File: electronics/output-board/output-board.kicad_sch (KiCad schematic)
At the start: 0 parts

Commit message: Added BSS806N library to the output board
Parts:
- added MOSFET?: BSS806NEH6327XTSA1, PG-SOT23-3-5_INF, symbol 2021-09-18_15-04-13:BSS806NEH6327XTSA1
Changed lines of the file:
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@@
 (kicad_sch (version 20210621) (generator eeschema)
   (paper "A4")
-  (symbol_instances)
+  (symbol (lib_id "2021-09-18_15-04-13:BSS806NEH6327XTSA1") (at 63.5 39.37 90) (unit 1)
+    (in_bom yes) (on_board yes) (fields_autoplaced)
+    (property "Reference" "MOSFET?" (id 0) (at 63.5 19.599 90)
+      (effects (font (size 1.524 1.524)))
+    )
+    (property "Value" "BSS806NEH6327XTSA1" (id 1) (at 63.5 22.878 90)
+      (effects (font (size 1.524 1.524)))
+    )
+    (property "Footprint" "PG-SOT23-3-5_INF" (id 2) (at 70.104 27.94 0)
+      (effects (font (size 1.524 1.524)) hide)
+    )
+    (property "Datasheet" "" (id 3) (at 63.5 39.37 0)
+      (effects (font (size 1.524 1.524)))
+    )
+    (pin "1")
+    (pin "2")
+    (pin "3")
+  )
+  (sheet_instances
+    (path "/" (page "1"))
+  )
+  (symbol_instances
+    (path "/b31e6aa4-4d79-4fd3-a6f6-5de1c4b80e42"
+      (reference "MOSFET?") (unit 1) (value "BSS806NEH6327XTSA1") (footprint "PG-SOT23-3-5_INF")
+    )
+  )
 )

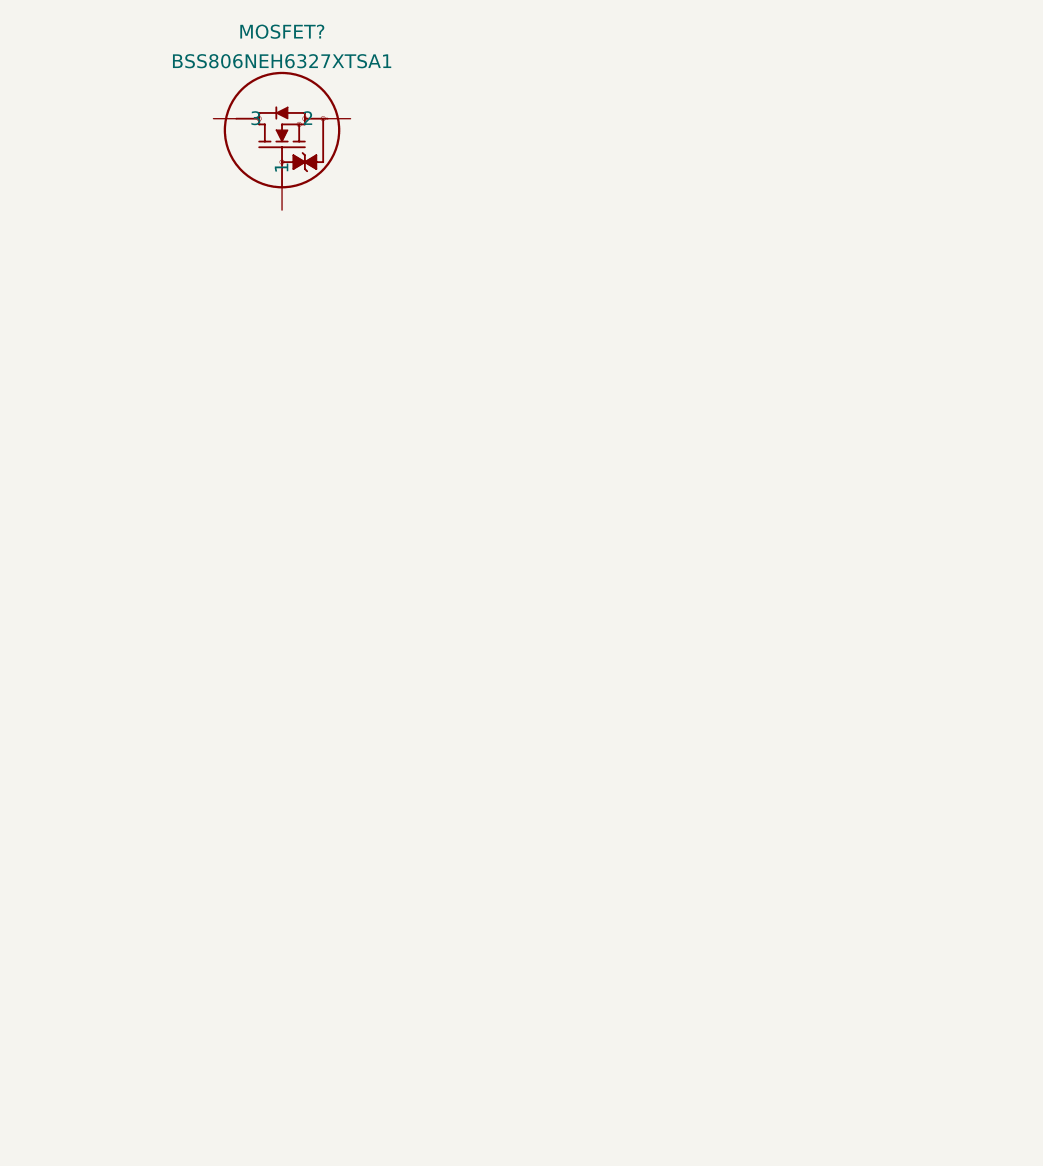
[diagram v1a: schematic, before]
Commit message: started working on output board
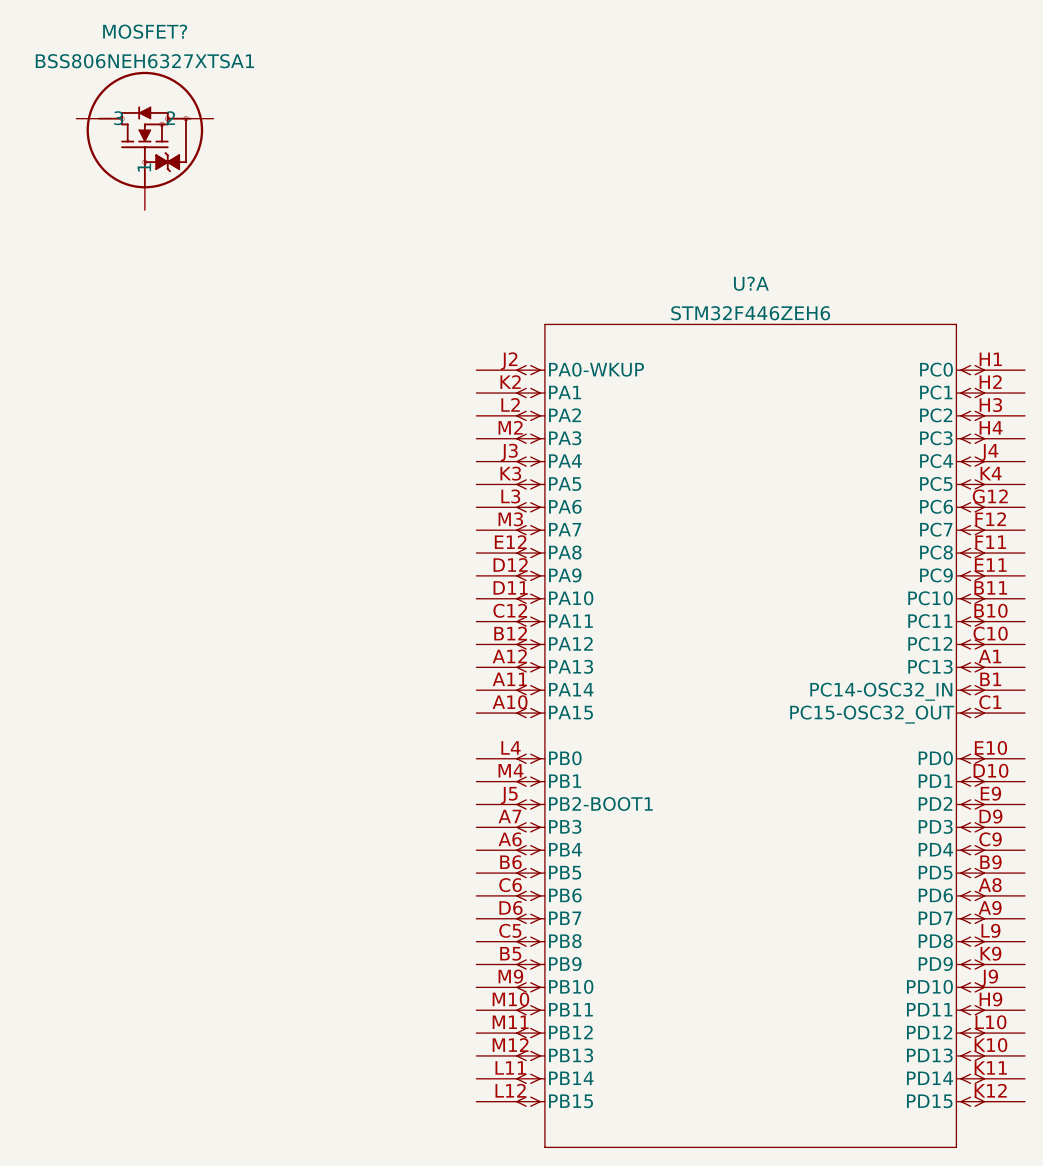
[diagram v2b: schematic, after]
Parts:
- added U?: STM32F446ZEH6, UFBGA144-7x7x0P6, symbol 2021-09-18_15-12-50:STM32F446ZEH6
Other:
- moved on the sheet: MOSFET?
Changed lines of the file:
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@@
 (kicad_sch (version 20210621) (generator eeschema)
   (paper "A4")
-  (symbol (lib_id "2021-09-18_15-04-13:BSS806NEH6327XTSA1") (at 63.5 39.37 90) (unit 1)
+  (symbol (lib_id "2021-09-18_15-04-13:BSS806NEH6327XTSA1") (at 48.26 39.37 90) (unit 1)
     (in_bom yes) (on_board yes) (fields_autoplaced)
-    (property "Reference" "MOSFET?" (id 0) (at 63.5 19.599 90)
+    (property "Reference" "MOSFET?" (id 0) (at 48.26 19.599 90)
       (effects (font (size 1.524 1.524)))
     )
-    (property "Value" "BSS806NEH6327XTSA1" (id 1) (at 63.5 22.878 90)
+    (property "Value" "BSS806NEH6327XTSA1" (id 1) (at 48.26 22.878 90)
       (effects (font (size 1.524 1.524)))
     )
-    (property "Footprint" "PG-SOT23-3-5_INF" (id 2) (at 70.104 27.94 0)
+    (property "Footprint" "PG-SOT23-3-5_INF" (id 2) (at 54.864 27.94 0)
       (effects (font (size 1.524 1.524)) hide)
     )
-    (property "Datasheet" "" (id 3) (at 63.5 39.37 0)
+    (property "Datasheet" "" (id 3) (at 48.26 39.37 0)
       (effects (font (size 1.524 1.524)))
     )
@@
     (pin "2")
     (pin "3")
+  )
+  (symbol (lib_id "2021-09-18_15-12-50:STM32F446ZEH6") (at 85.09 57.15 0) (unit 1)
+    (in_bom yes) (on_board yes) (fields_autoplaced)
+    (property "Reference" "U?" (id 0) (at 115.57 47.6025 0)
+      (effects (font (size 1.524 1.524)))
+    )
+    (property "Value" "STM32F446ZEH6" (id 1) (at 115.57 50.8815 0)
+      (effects (font (size 1.524 1.524)))
+    )
+    (property "Footprint" "UFBGA144-7x7x0P6" (id 2) (at 115.57 51.054 0)
+      (effects (font (size 1.524 1.524)) hide)
+    )
+    (property "Datasheet" "" (id 3) (at 85.09 57.15 0)
+      (effects (font (size 1.524 1.524)))
+    )
+    (pin "A1")
+    (pin "A10")
+    (pin "A11")
+    (pin "A12")
+    (pin "A6")
+    (pin "A7")
+    (pin "A8")
+    (pin "A9")
+    (pin "B1")
+    (pin "B10")
+    (pin "B11")
+    (pin "B12")
+    (pin "B5")
+    (pin "B6")
+    (pin "B9")
+    (pin "C1")
+    (pin "C10")
+    (pin "C12")
+    (pin "C5")
+    (pin "C6")
+    (pin "C9")
+    (pin "D10")
+    (pin "D11")
+    (pin "D12")
+    (pin "D6")
+    (pin "D9")
+    (pin "E10")
+    (pin "E11")
+    (pin "E12")
+    (pin "E9")
+    (pin "F11")
+    (pin "F12")
+    (pin "G12")
+    (pin "H1")
+    (pin "H2")
+    (pin "H3")
+    (pin "H4")
+    (pin "H9")
+    (pin "J2")
+    (pin "J3")
+    (pin "J4")
+    (pin "J5")
+    (pin "J9")
+    (pin "K10")
+    (pin "K11")
+    (pin "K12")
+    (pin "K2")
+    (pin "K3")
+    (pin "K4")
+    (pin "K9")
+    (pin "L10")
+    (pin "L11")
+    (pin "L12")
+    (pin "L2")
+    (pin "L3")
+    (pin "L4")
+    (pin "L9")
+    (pin "M10")
+    (pin "M11")
+    (pin "M12")
+    (pin "M2")
+    (pin "M3")
+    (pin "M4")
+    (pin "M9")
   )
   (sheet_instances
@@
       (reference "MOSFET?") (unit 1) (value "BSS806NEH6327XTSA1") (footprint "PG-SOT23-3-5_INF")
     )
+    (path "/e354fa5f-e405-4e62-b4d4-c6e5e046a118"
+      (reference "U?") (unit 1) (value "STM32F446ZEH6") (footprint "UFBGA144-7x7x0P6")
+    )
   )

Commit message: Added MOSFETS to the output board.
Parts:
- removed U?: STM32F446ZEH6, UFBGA144-7x7x0P6, symbol 2021-09-18_15-12-50:STM32F446ZEH6
- added D?: LED, symbol Device:LED
- added J1, J? (x16): Conn_01x02_Male, symbol Connector:Conn_01x02_Male
- added MOSFET? (x16): BSS806NEH6327XTSA1, PG-SOT23-3-5_INF, symbol 2021-09-18_15-04-13:BSS806NEH6327XTSA1
- added Q?: 2N2219, Package_TO_SOT_THT:TO-39-3, symbol Transistor_BJT:2N2219
- added R? (x18): R, symbol Device:R
- gave numbers to parts that had none: 1
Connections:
- net at MOSFET1.1: now also Q?.2 (B), R?.1
- net GND: now reaches MOSFET1.2
- net GND: now also MOSFET?.2, MOSFET?.2, MOSFET?.2, MOSFET?.2, MOSFET?.2, MOSFET?.2, MOSFET?.2, MOSFET?.2, MOSFET?.2, MOSFET?.2, MOSFET?.2, MOSFET?.2, MOSFET?.2, R?.2
- net at MOSFET1.3: now also J1.1 (Pin_1)
- new net: MOSFET?.1, R?.1 (x16)
- new net: J?.1 (Pin_1), MOSFET?.3 (x15)
- new net: Q?.1 (E), R?.1
- new net: MOSFET?.2, MOSFET?.2, MOSFET?.2, MOSFET?.3
- new net: J?.1 (Pin_1), R?.2
- new net: D?.1 (K), Q?.3 (C)
- new net +12V: J1.2 (Pin_2), J?.2 (Pin_2), J?.2 (Pin_2), J?.2 (Pin_2), J?.2 (Pin_2), J?.2 (Pin_2), J?.2 (Pin_2), J?.2 (Pin_2), J?.2 (Pin_2), J?.2 (Pin_2), J?.2 (Pin_2), J?.2 (Pin_2), J?.2 (Pin_2), J?.2 (Pin_2), J?.2 (Pin_2), J?.2 (Pin_2)
- new net +5V: D?.2 (A)
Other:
- note added: "Arming Switch"
- note added: "Do I need a pulldown resistor?"
- moved on the sheet: MOSFET1

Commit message: Finished Schematic and Started Routing the Output Board
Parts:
- removed D?: LED, symbol Device:LED
- removed J1, J? (x16): Conn_01x02_Male, symbol Connector:Conn_01x02_Male
- removed MOSFET1, MOSFET? (x16): BSS806NEH6327XTSA1, PG-SOT23-3-5_INF, symbol 2021-09-18_15-04-13:BSS806NEH6327XTSA1
- removed Q?: 2N2219, Package_TO_SOT_THT:TO-39-3, symbol Transistor_BJT:2N2219
- removed R? (x18): R, symbol Device:R
- added C1, C3: 1uF, Capacitor_SMD:C_0603_1608Metric, symbol Device:C_Small
- added C10, C11, C12, C13, C14, C15, C16, C17, C18, C19, C20, C21, C6, C9: 100nF, Capacitor_SMD:C_0603_1608Metric, symbol Device:C_Small
- added C2: 10nF, Capacitor_SMD:C_0603_1608Metric, symbol Device:C_Small
- added C4, C5: 20pF, Capacitor_SMD:C_0603_1608Metric, symbol Device:C_Small
- added C7, C8: 2.2uF, Capacitor_SMD:C_0603_1608Metric, symbol Device:C_Small
- added J14: Arming switch, Connector_PinHeader_2.54mm:PinHeader_1x02_P2.54mm_Vertical, symbol Connector:Conn_01x02_Male
- added J3: 12V In, Connector_PinHeader_2.54mm:PinHeader_1x02_P2.54mm_Vertical, symbol Connector:Conn_01x02_Male
- added J4, J6: Conn_01x02, Connector_PinHeader_2.54mm:PinHeader_1x02_P2.54mm_Vertical, symbol Connector_Generic:Conn_01x02
- added J5: SWD Header, Connector_PinHeader_2.54mm:PinHeader_1x04_P2.54mm_Vertical, symbol Connector_Generic:Conn_01x04
- added L1: 10uH, Inductor_SMD:L_0603_1608Metric, symbol Device:L_Core_Iron
- added MOSFET10: BUK9Y21-40E, MOSFET 2:BUK9Y21-40E, symbol ArmingMOSFET:BUK9Y21-40E
- added R1: 0k, Resistor_SMD:R_0603_1608Metric, symbol Device:R_Small
- added R12: 1K, Resistor_SMD:R_0603_1608Metric, symbol Device:R
- added R13: 100K, Resistor_SMD:R_0603_1608Metric, symbol Device:R
- added R3: 10k, Resistor_SMD:R_0603_1608Metric, symbol Device:R_Small
- added SW1: SW_Push_Dual, RESET BUTTON:Button CS1102, symbol Switch:SW_Push_Dual
- added U1: MAX33012EASA+, MAX33012EASA+:MAX33012EASA+, symbol MAX33012EASA+:MAX33012EASA+
- added U2: LD3985M33R_SOT23, Package_TO_SOT_SMD:SOT-23-5, symbol Regulator_Linear:LD3985M33R_SOT23
- added U3: STM32F446ZEHx, Package_BGA:UFBGA-144_7x7mm_Layout12x12_P0.5mm, symbol MCU_ST_STM32F4:STM32F446ZEHx
- added Y1: 25MHz 9pF, symbol Device:Crystal_Small
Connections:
- net +12V: now also J3.2 (Pin_2)
- net +5V: now also C1.1, J14.2 (Pin_2), J4.1 (Pin_1), J5.2 (Pin_2), U2.1 (VIN), U2.3 (INH)
- net GND: now also C1.2, C10.2, C11.2, C12.2, C13.2, C14.2, C15.2, C16.2, C17.2, C18.2, C19.2, C2.2, C20.2, C21.2, C3.2, C4.1, C5.1, C6.1, C7.2, C8.2, C9.2, J3.1 (Pin_1), J4.2 (Pin_2), J5.1 (Pin_1), MOSFET10.1, MOSFET10.2, MOSFET10.3, R13.2, R3.2, SW1.1, SW1.3, U1.2 (GND), U1.8 (STBY), U2.2 (GND), U3.D2 (VSS), U3.E6 (VSS), U3.E7 (VSS), U3.G10 (VSS), U3.G4 (VSS), U3.G8 (VSS), U3.H6 (VSS), U3.J1 (VSSA), U3.K1 (VREF-)
- new net: MOSFET10.4, R12.1
- new net: C6.2, SW1.2, SW1.4, U3.F1 (NRST)
- new net: J14.1 (Pin_1), R12.2, R13.1, U3.C3 (PF0)
- new net: J6.2 (Pin_2), U1.6 (CANL)
- new net: J6.1 (Pin_1), U1.7 (CANH)
- new net: C5.2, U3.E1 (PH1), Y1.1
- new net: C2.1, U2.4 (BYP)
- new net: C4.2, R1.1, Y1.2
- new net: R3.1, U3.D5 (BOOT0)
- new net: C8.1, U3.G9 (VCAP_2)
- new net: C7.1, U3.H7 (VCAP_1)
- new net: R1.2, U3.D1 (PH0)
- new net +3V3: C11.1, C12.1, C13.1, C14.1, C15.1, C16.1, C17.1, C18.1, C19.1, C20.1, C21.1, C3.1, C9.1, L1.2, U1.3 (VDD), U2.5 (VOUT), U3.C2 (VBAT), U3.D3 (VDD), U3.E5 (PDR_ON), U3.F10 (VDD), U3.F4 (VDD), U3.F5 (VDD), U3.F6 (VDD), U3.F7 (VDD), U3.F8 (VDD), U3.F9 (VDD), U3.G5 (VDD), U3.G6 (VDD), U3.G7 (VDD)
- new net CAN_RX: U1.4 (RXD), U3.E10 (PD0)
- new net CAN_TX: U1.1 (TXD), U3.D10 (PD1)
- new net Ignition MOSFET/GROUND: MOSFET10.5
- new net Ignition MOSFET/INPUT: U3.B8 (PG12)
- new net MOSFET-sheet/INPUT: U3.K6 (PG0)
- new net MOSFET-sheet1/INPUT: U3.J6 (PG1)
- new net MOSFET-sheet10/INPUT: U3.D8 (PG10)
- new net MOSFET-sheet11/INPUT: U3.C8 (PG11)
- new net MOSFET-sheet2/INPUT: U3.J12 (PG2)
- new net MOSFET-sheet3/INPUT: U3.J11 (PG3)
- new net MOSFET-sheet4/INPUT: U3.J10 (PG4)
- new net MOSFET-sheet5/INPUT: U3.H12 (PG5)
- new net MOSFET-sheet6/INPUT: U3.H11 (PG6)
- new net MOSFET-sheet7/INPUT: U3.H10 (PG7)
- new net MOSFET-sheet8/INPUT: U3.G11 (PG8)
- new net MOSFET-sheet9/INPUT: U3.E8 (PG9)
- new net SWCLK: J5.3 (Pin_3), U3.A11 (PA14)
- new net SWDIO: J5.4 (Pin_4), U3.A12 (PA13)
- new net VDDA: C10.1, L1.1, U3.L1 (VREF+), U3.M1 (VDDA)
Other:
- added sheet Ignition MOSFET (untitled.kicad_sch)
- added sheet MOSFET-sheet (untitled.kicad_sch)
- added sheet MOSFET-sheet1 (untitled.kicad_sch)
- added sheet MOSFET-sheet10 (untitled.kicad_sch)
- added sheet MOSFET-sheet11 (untitled.kicad_sch)
- added sheet MOSFET-sheet2 (untitled.kicad_sch)
- added sheet MOSFET-sheet3 (untitled.kicad_sch)
- added sheet MOSFET-sheet4 (untitled.kicad_sch)
- added sheet MOSFET-sheet5 (untitled.kicad_sch)
- added sheet MOSFET-sheet6 (untitled.kicad_sch)
- added sheet MOSFET-sheet7 (untitled.kicad_sch)
- added sheet MOSFET-sheet8 (untitled.kicad_sch)
- added sheet MOSFET-sheet9 (untitled.kicad_sch)
- note added: "Each VDD pin should be connected to a decoupling capacitor as closely as possible to the pin"
- note added: "Hardcode to boot from flash memory"
- note added: "Should be ceramic capacitors (low ESR)"
- note added: "To Do: -Servo Valve Control? -Layout Board -Get Footprints"
- note removed: "Arming Switch"
- note removed: "Do I need a pulldown resistor?"

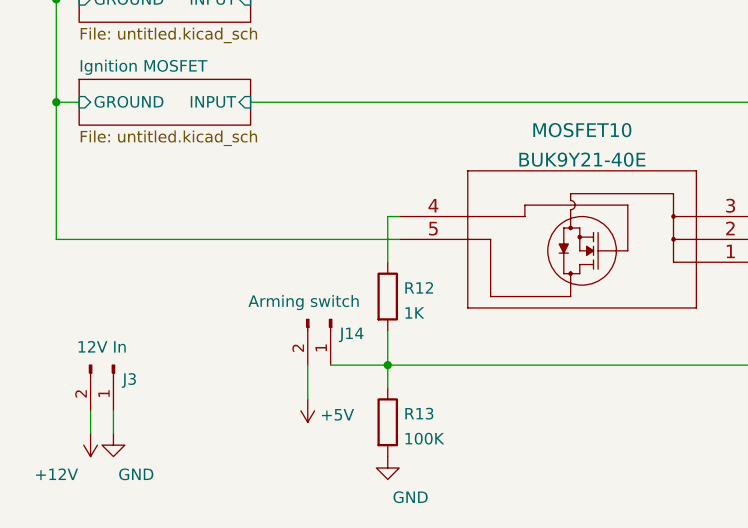
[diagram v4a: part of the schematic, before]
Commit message: Working on ouput board.
Saving before using the replicate layout plugin.
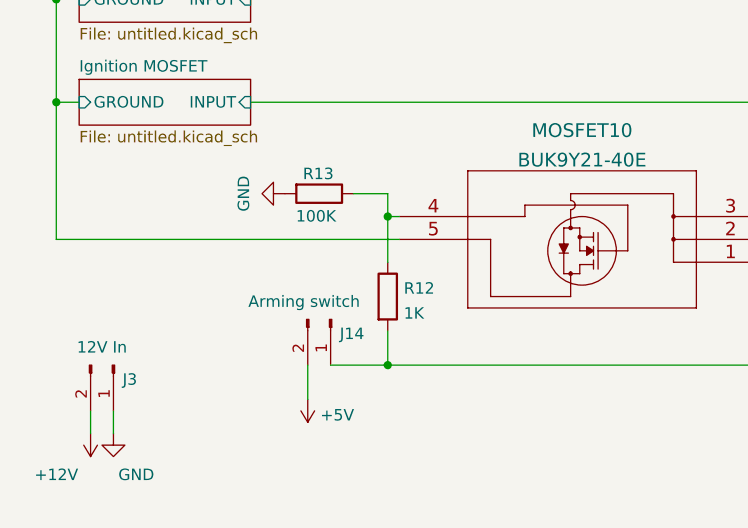
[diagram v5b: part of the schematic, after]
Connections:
- net at MOSFET10.4, R12.1: now also R13.1
- net at J14.1 (Pin_1), R12.2, U3.C3 (PF0): no longer R13.1
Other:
- moved on the sheet: R13
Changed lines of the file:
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@@
   (junction (at 53.34 55.88) (diameter 1.016) (color 0 0 0 0))
   (junction (at 62.23 55.88) (diameter 1.016) (color 0 0 0 0))
+  (junction (at 63.5 302.26) (diameter 0) (color 0 0 0 0))
   (junction (at 63.5 318.77) (diameter 0) (color 0 0 0 0))
   (junction (at 69.85 45.72) (diameter 0) (color 0 0 0 0))
@@
     (stroke (width 0) (type default) (color 0 0 0 0))
   )
+  (wire (pts (xy 59.69 299.72) (xy 63.5 299.72))
+    (stroke (width 0) (type default) (color 0 0 0 0))
+  )
   (wire (pts (xy 60.96 45.72) (xy 69.85 45.72))
     (stroke (width 0) (type solid) (color 0 0 0 0))
@@
     (stroke (width 0) (type solid) (color 0 0 0 0))
   )
+  (wire (pts (xy 63.5 299.72) (xy 63.5 302.26))
+    (stroke (width 0) (type default) (color 0 0 0 0))
+  )
   (wire (pts (xy 63.5 302.26) (xy 63.5 307.34))
     (stroke (width 0) (type default) (color 0 0 0 0))
@@
   )
   (wire (pts (xy 63.5 314.96) (xy 63.5 318.77))
-    (stroke (width 0) (type default) (color 0 0 0 0))
-  )
-  (wire (pts (xy 63.5 318.77) (xy 63.5 321.31))
     (stroke (width 0) (type default) (color 0 0 0 0))
   )
@@
     (pin "1")
   )
+  (symbol (lib_id "power:GND") (at 52.07 299.72 270) (unit 1)
+    (in_bom yes) (on_board yes)
+    (property "Reference" "#PWR0103" (id 0) (at 45.72 299.72 0)
+      (effects (font (size 1.27 1.27)) hide)
+    )
+    (property "Value" "GND" (id 1) (at 47.5074 299.72 0))
+    (property "Footprint" "" (id 2) (at 52.07 299.72 0)
+      (effects (font (size 1.27 1.27)) hide)
+    )
+    (property "Datasheet" "" (id 3) (at 52.07 299.72 0)
+      (effects (font (size 1.27 1.27)) hide)
+    )
+    (pin "1")
+  )
   (symbol (lib_id "power:GND") (at 53.34 55.88 0) (unit 1)
     (in_bom yes) (on_board yes) (fields_autoplaced)
@@
     )
     (property "Datasheet" "" (id 3) (at 57.15 109.22 0)
-      (effects (font (size 1.27 1.27)) hide)
-    )
-    (pin "1")
-  )
-  (symbol (lib_id "power:GND") (at 63.5 328.93 0) (unit 1)
-    (in_bom yes) (on_board yes)
-    (property "Reference" "#PWR0103" (id 0) (at 63.5 335.28 0)
-      (effects (font (size 1.27 1.27)) hide)
-    )
-    (property "Value" "GND" (id 1) (at 66.04 333.4926 0))
-    (property "Footprint" "" (id 2) (at 63.5 328.93 0)
-      (effects (font (size 1.27 1.27)) hide)
-    )
-    (property "Datasheet" "" (id 3) (at 63.5 328.93 0)
       (effects (font (size 1.27 1.27)) hide)
     )
@@
     (pin "2")
   )
+  (symbol (lib_id "Device:R") (at 55.88 299.72 270) (unit 1)
+    (in_bom yes) (on_board yes)
+    (property "Reference" "R13" (id 0) (at 54.0706 297.5136 90)
+      (effects (font (size 1.27 1.27)) (justify left))
+    )
+    (property "Value" "100K" (id 1) (at 53.2924 302.2267 90)
+      (effects (font (size 1.27 1.27)) (justify left))
+    )
+    (property "Footprint" "Resistor_SMD:R_0603_1608Metric" (id 2) (at 55.88 297.942 90)
+      (effects (font (size 1.27 1.27)) hide)
+    )
+    (property "Datasheet" "~" (id 3) (at 55.88 299.72 0)
+      (effects (font (size 1.27 1.27)) hide)
+    )
+    (pin "1")
+    (pin "2")
+  )
   (symbol (lib_id "Device:R") (at 63.5 311.15 0) (unit 1)
     (in_bom yes) (on_board yes) (fields_autoplaced)
@@
       (effects (font (size 1.27 1.27)) hide)
     )
-    (pin "1")
-    (pin "2")
-  )
-  (symbol (lib_id "Device:R") (at 63.5 325.12 0) (unit 1)
-    (in_bom yes) (on_board yes) (fields_autoplaced)
-    (property "Reference" "R13" (id 0) (at 65.2781 324.2115 0)
-      (effects (font (size 1.27 1.27)) (justify left))
-    )
-    (property "Value" "100K" (id 1) (at 65.2781 326.9866 0)
-      (effects (font (size 1.27 1.27)) (justify left))
-    )
-    (property "Footprint" "Resistor_SMD:R_0603_1608Metric" (id 2) (at 61.722 325.12 90)
-      (effects (font (size 1.27 1.27)) hide)
-    )
-    (property "Datasheet" "~" (id 3) (at 63.5 325.12 0)
-      (effects (font (size 1.27 1.27)) hide)
-    )
